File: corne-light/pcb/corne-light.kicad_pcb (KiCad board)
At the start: 2 copper layers, 275.5 x 105.6 mm, 118 parts, among them J1 MJ-4PP-9, J2 OLED, J5 Breakaway_Tabs, J6 MJ-4PP-9, J7 OLED, SW1 SW_PUSH, SW10 SW_PUSH, SW11 SW_PUSH, SW12 SW_PUSH, SW13 SW_PUSH, SW14 SW_PUSH, SW15 SW_PUSH, SW16 SW_PUSH, SW17 SW_PUSH, SW18 SW_PUSH, SW19 SW_PUSH, SW2 SW_PUSH, SW20 SW_PUSH, SW21 SW_PUSH, SW22 SW_PUSH, SW23 SW_PUSH, SW24 SW_PUSH, SW25 SW_PUSH, SW26 SW_PUSH, SW27 SW_PUSH, SW28 SW_PUSH, SW29 SW_PUSH, SW3 SW_PUSH, SW30 SW_PUSH, SW31 SW_PUSH, SW32 SW_PUSH, SW33 SW_PUSH, SW34 SW_PUSH, SW35 SW_PUSH, SW36 SW_PUSH, SW37 SW_PUSH, SW38 SW_PUSH, SW39 SW_PUSH, SW4 SW_PUSH, SW40 SW_PUSH, SW41 SW_PUSH, SW42 SW_PUSH, SW5 SW_PUSH, SW6 SW_PUSH, SW7 SW_PUSH, SW8 SW_PUSH, SW9 SW_PUSH, U1 ProMicro, U2 ProMicro

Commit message: Update board
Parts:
- D1, D10, D11, D12, D13, D14, D15, D16, D17, D18, D19, D2, D20, D21, D22, D23, D24, D25, D26, D27, D28, D29, D3, D30, D31, D32, D33, D34, D35, D36, D37, D38, D39, D4, D40, D41, D42, D5, D6, D7, D8, D9: footprint kbd:D3_TH -> kbd:D3_SMD_v2
- Ref** (x4): footprint kbd:M2_Threads_v2 -> kbd:thread_m2
- Ref** (x10): footprint kbd:M2_Threads_v2 -> kbd:spacer_m2
- SW1, SW10, SW11, SW12, SW13, SW14, SW15, SW16, SW17, SW18, SW19, SW2, SW20, SW22, SW23, SW24, SW25, SW26, SW27, SW28, SW29, SW3, SW30, SW31, SW32, SW33, SW34, SW35, SW36, SW37, SW38, SW39, SW4, SW40, SW41, SW5, SW6, SW7, SW8, SW9: footprint kbd:CherryMX_ChocV2_1u -> kbd:keyswitch_cherrymx_alps_choc12_1u
- SW21, SW42: footprint kbd:CherryMX_ChocV2_1.5u -> kbd:keyswitch_cherrymx_alps_choc12_1.5u
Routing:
- net row2: track 141.0 -> 149.0 mm
- net Net-(D16-Pad2): track 27.0 -> 34.5 mm
- net row3: track 96.9 -> 90.6 mm
- net row3_r: track 86.2 -> 81.5 mm
- net row1: track 155.9 -> 160.3 mm
- net row0: track 134.2 -> 137.4 mm
- net col0_r: track 186.3 -> 183.2 mm
- net col0: track 180.2 -> 182.3 mm
- net row0_r: track 124.4 -> 122.9 mm
- net Net-(D27-Pad2): track 20.5 -> 19.3 mm
- net Net-(D10-Pad2): track 26.7 -> 27.9 mm
- net Net-(D33-Pad2): track 20.4 -> 19.2 mm
- net Net-(D39-Pad2): track 19.8 -> 18.6 mm
- net row2_r: track 131.5 -> 132.7 mm
- net Net-(D4-Pad2): track 26.7 -> 27.8 mm
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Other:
- outline, holes or cut-outs redrawn
- net class Min added: clearance 0.00001, trace_width 0.2, via_dia 0.4, via_drill 0.3

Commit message: Update pcb
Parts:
- D1, D10, D11, D12, D13, D14, D15, D16, D17, D18, D19, D2, D20, D21, D22, D23, D24, D25, D26, D27, D28, D29, D3, D30, D31, D32, D33, D34, D35, D36, D37, D38, D39, D4, D40, D41, D42, D5, D6, D7, D8, D9: footprint kbd:D3_SMD_v2 -> kbd:D3_TH_SMD_v2
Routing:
- net row2: track 149.0 -> 153.9 mm
- net row2_r: track 132.7 -> 137.6 mm
- net row1_r: track 129.4 -> 134.3 mm
- net row0: track 137.4 -> 142.3 mm
- net row0_r: track 122.9 -> 127.8 mm
- net row3: track 90.6 -> 94.6 mm
- net row3_r: track 81.5 -> 85.2 mm
- net row1: track 160.3 -> 164.0 mm
- net Net-(D42-Pad2): track 46.6 -> 47.8 mm
- net Net-(D37-Pad2): track 21.1 -> 22.3 mm
- net Net-(D19-Pad2): track 26.8 -> 28.1 mm
- net Net-(D9-Pad2): track 19.9 -> 21.1 mm
- net Net-(D8-Pad2): track 26.0 -> 27.2 mm
- net Net-(D7-Pad2): track 20.1 -> 21.3 mm
- net Net-(D6-Pad2): track 25.3 -> 26.5 mm
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
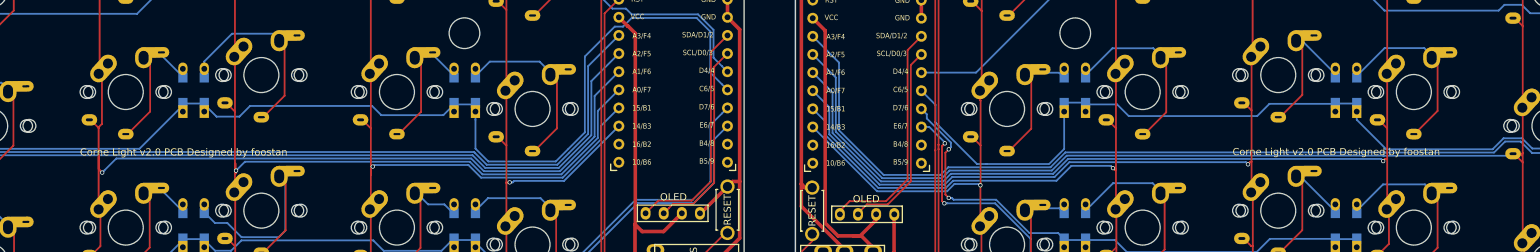
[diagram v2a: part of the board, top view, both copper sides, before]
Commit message: Add add holes for mini
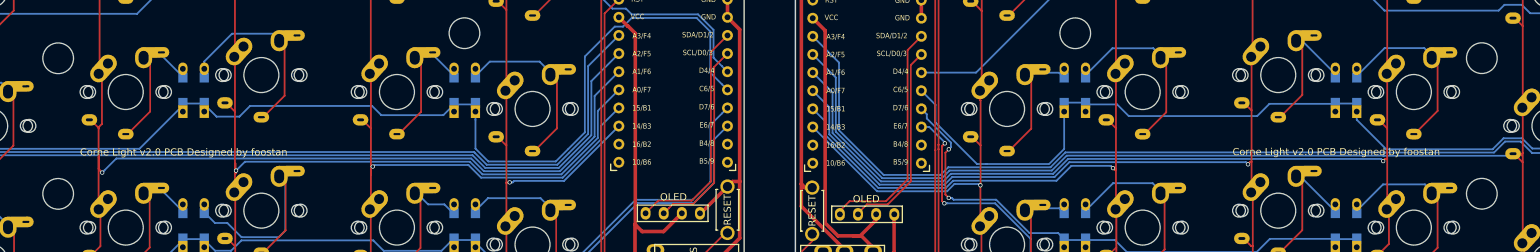
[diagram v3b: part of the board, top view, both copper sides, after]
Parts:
- added Ref**: Val**, kbd:spacer_m2, B.Cu at (250.2, 55.4)
- added Ref**: Val**, kbd:spacer_m2, B.Cu at (250.2, 74.4)
- added Ref**: Val**, kbd:spacer_m2, B.Cu at (50.7, 55.4)
- added Ref**: Val**, kbd:spacer_m2, B.Cu at (50.7, 74.4)
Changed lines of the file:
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@@
     (tracks 1240)
     (zones 0)
-    (modules 118)
+    (modules 122)
     (nets 89)
   )
@@
     (pad_to_mask_clearance 0.2)
     (aux_axis_origin 74.8395 91.6855)
-    (grid_origin 31.6975 55.41)
+    (grid_origin 31.7125 74.445)
     (visible_elements FFFFFF7F)
     (pcbplotparams
@@
     (diff_pair_gap 0.00001)
   )
+  (module kbd:spacer_m2 (layer B.Cu)
+    (at 250.2125 55.426932 180)
+    (descr "Mounting Hole 2.2mm, no annular, M2")
+    (tags "mounting hole 2.2mm no annular m2")
+    (attr virtual)
+    (fp_text reference Ref** (at -0.95 0.55) (layer B.Fab) hide
+      (effects (font (size 1 1) (thickness 0.15)) (justify mirror))
+    )
+    (fp_text value Val** (at 0 -0.55) (layer B.Fab) hide
+      (effects (font (size 1 1) (thickness 0.15)) (justify mirror))
+    )
+    (pad "" np_thru_hole circle (at 0 0 180) (size 4.3 4.3) (drill 4.3) (layers *.Cu *.Mask))
+  )
+  (module kbd:spacer_m2 (layer B.Cu)
+    (at 250.2125 74.426932 180)
+    (descr "Mounting Hole 2.2mm, no annular, M2")
+    (tags "mounting hole 2.2mm no annular m2")
+    (attr virtual)
+    (fp_text reference Ref** (at -0.95 0.55) (layer B.Fab) hide
+      (effects (font (size 1 1) (thickness 0.15)) (justify mirror))
+    )
+    (fp_text value Val** (at 0 -0.55) (layer B.Fab) hide
+      (effects (font (size 1 1) (thickness 0.15)) (justify mirror))
+    )
+    (pad "" np_thru_hole circle (at 0 0 180) (size 4.3 4.3) (drill 4.3) (layers *.Cu *.Mask))
+  )
+  (module kbd:spacer_m2 (layer B.Cu)
+    (at 50.7125 55.445 180)
+    (descr "Mounting Hole 2.2mm, no annular, M2")
+    (tags "mounting hole 2.2mm no annular m2")
+    (attr virtual)
+    (fp_text reference Ref** (at -0.95 0.55) (layer B.Fab) hide
+      (effects (font (size 1 1) (thickness 0.15)) (justify mirror))
+    )
+    (fp_text value Val** (at 0 -0.55) (layer B.Fab) hide
+      (effects (font (size 1 1) (thickness 0.15)) (justify mirror))
+    )
+    (pad "" np_thru_hole circle (at 0 0 180) (size 4.3 4.3) (drill 4.3) (layers *.Cu *.Mask))
+  )
+  (module kbd:spacer_m2 (layer B.Cu)
+    (at 50.7125 74.445 180)
+    (descr "Mounting Hole 2.2mm, no annular, M2")
+    (tags "mounting hole 2.2mm no annular m2")
+    (attr virtual)
+    (fp_text reference Ref** (at -0.95 0.55) (layer B.Fab) hide
+      (effects (font (size 1 1) (thickness 0.15)) (justify mirror))
+    )
+    (fp_text value Val** (at 0 -0.55) (layer B.Fab) hide
+      (effects (font (size 1 1) (thickness 0.15)) (justify mirror))
+    )
+    (pad "" np_thru_hole circle (at 0 0 180) (size 4.3 4.3) (drill 4.3) (layers *.Cu *.Mask))
+  )
   (module kbd:D3_TH_SMD_v2 (layer B.Cu)

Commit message: light
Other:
- net class Default removed
- net class Min removed
